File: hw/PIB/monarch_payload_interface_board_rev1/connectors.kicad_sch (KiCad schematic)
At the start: 14 parts, among them J1 5037630291, J10 5037630491, J11 5037630691, J12 5037630691, J13 5037630491, J14 5037630491, J2 5037630291, J3 5037630691, J4 5037630691, J5 5037630691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

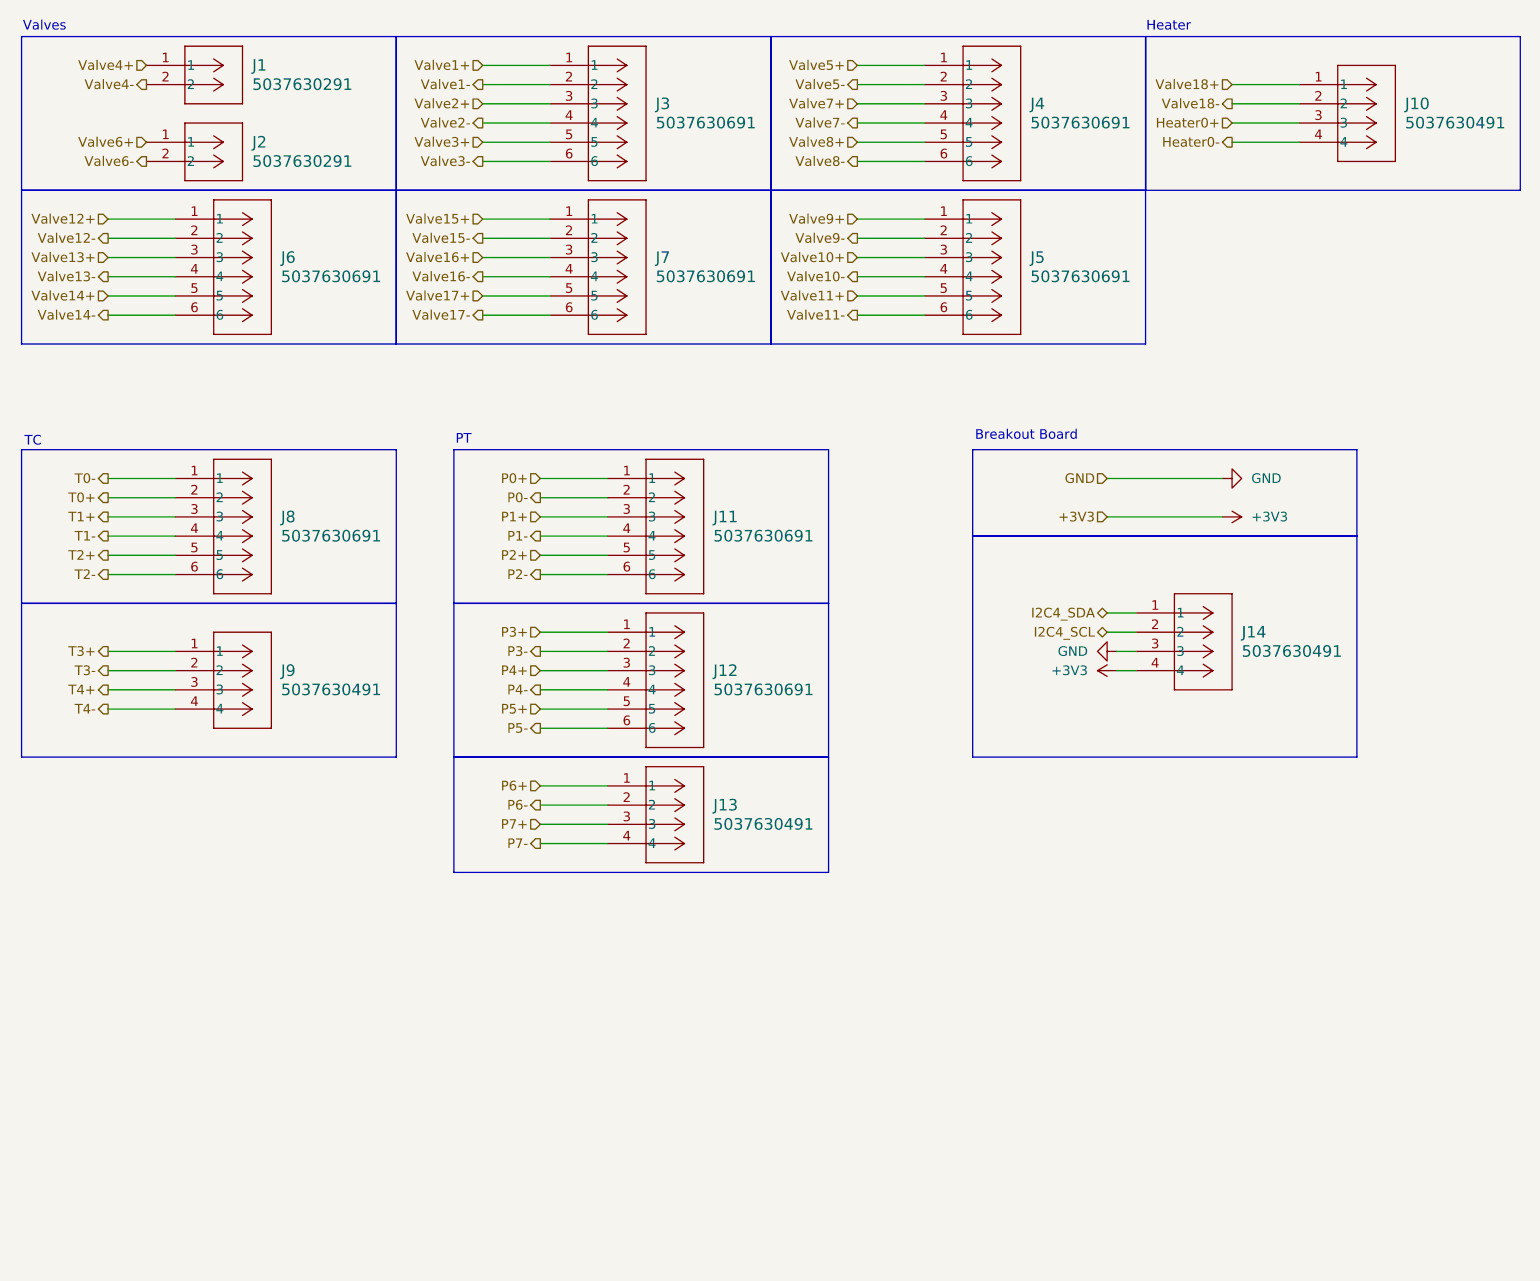
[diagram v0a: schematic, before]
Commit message: PIB layout update
done pending Ben O approval
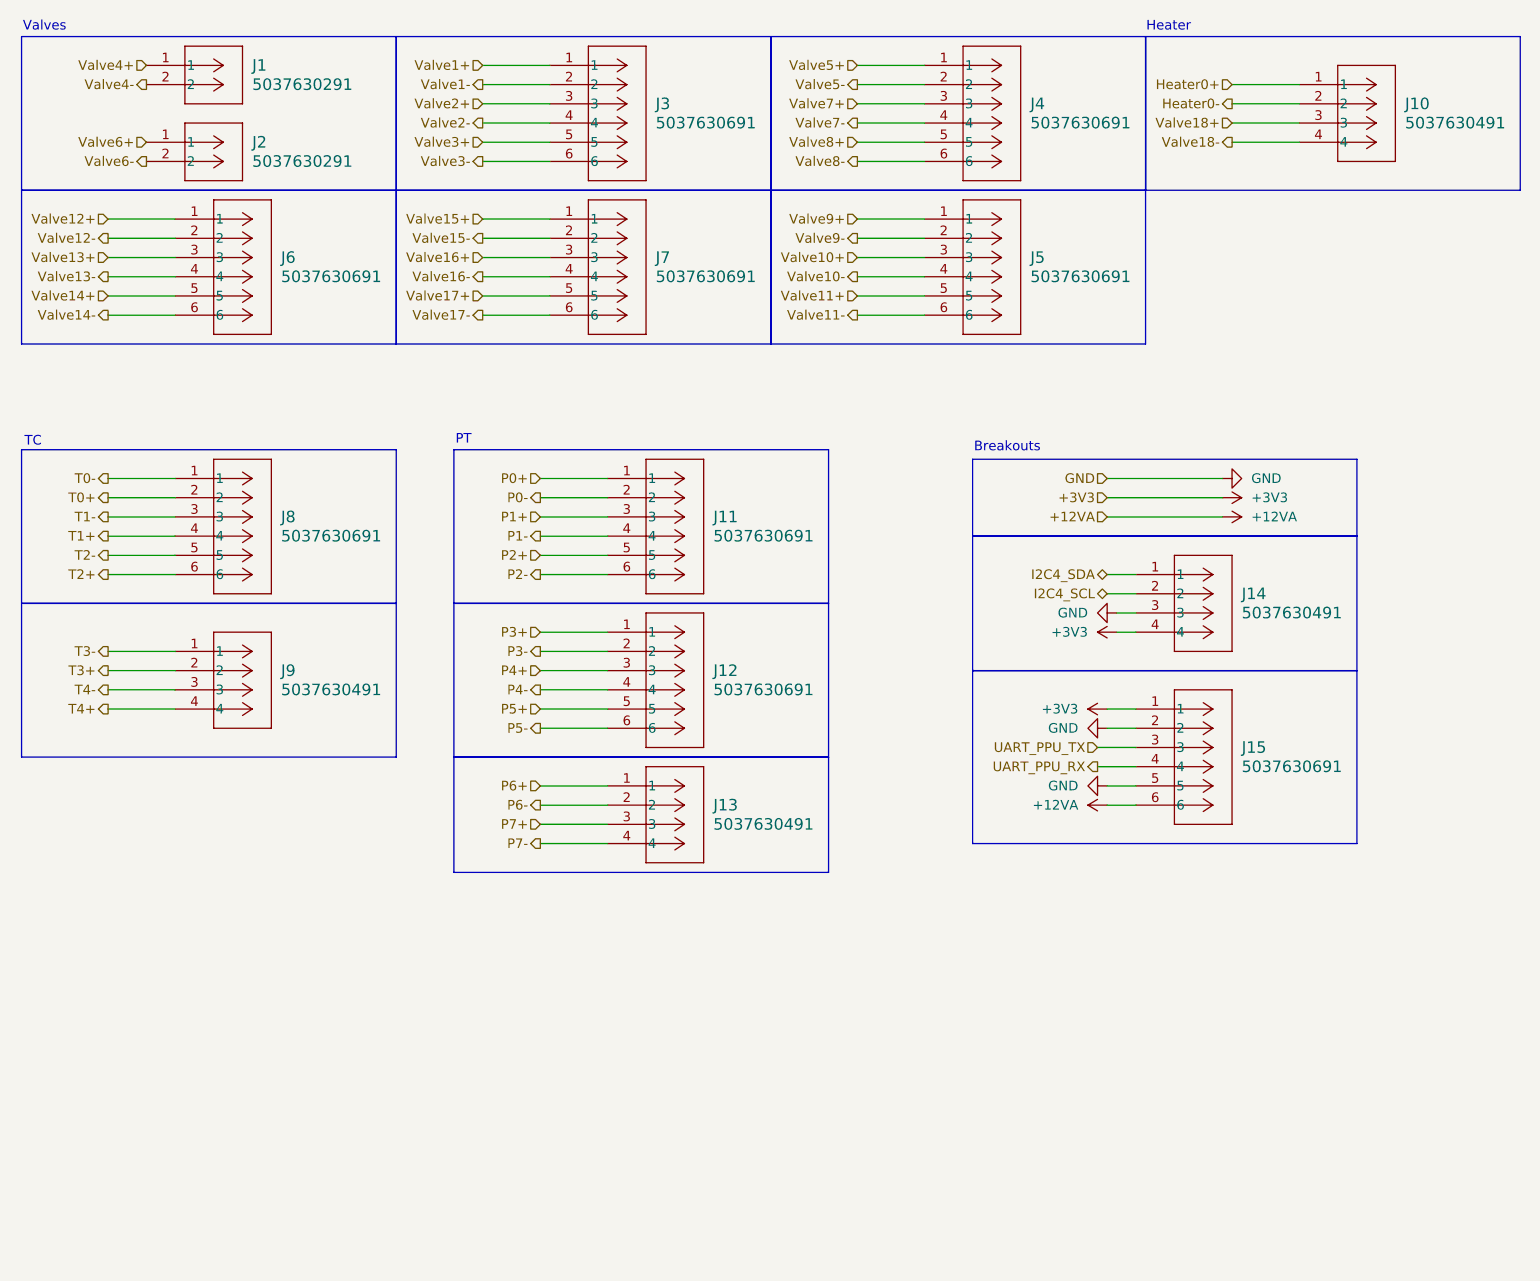
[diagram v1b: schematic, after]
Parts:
- added J15: 5037630691, CONN_5037630000-SD_06_MOL, symbol 5037630691:5037630691
- J10: footprint CONN_5037630000-SD_04_MOL -> 5037630491:CONN_5037630000-SD_04_MOL
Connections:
- net +3V3: now also J15.1
- net GND: now also J15.2, J15.5
- net Heater0+: now also J10.1; no longer J10.3
- net Heater0-: now also J10.2; no longer J10.4
- net T1+: now also J8.4; no longer J8.3
- net T1-: now also J8.3; no longer J8.4
- net T2+: now also J8.6; no longer J8.5
- net T2-: now also J8.5; no longer J8.6
- net T3+: now also J9.2; no longer J9.1
- net T3-: now also J9.1; no longer J9.2
- net T4+: now also J9.4; no longer J9.3
- net T4-: now also J9.3; no longer J9.4
- net Valve18+: now also J10.3; no longer J10.1
- net Valve18-: now also J10.4; no longer J10.2
- new net +12VA: J15.6
- new net UART_PPU_RX: J15.4
- new net UART_PPU_TX: J15.3
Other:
- note added: "Breakouts"
- note removed: "Breakout Board"
- moved on the sheet: J14

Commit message: PIB minor updates & radio board
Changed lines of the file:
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@@
 	)
 	(hierarchical_label "UART_PPU_RX"
-		(shape output)
+		(shape input)
 		(at 166.37 116.84 180)
 		(effects
@@
 	)
 	(hierarchical_label "UART_PPU_TX"
-		(shape input)
+		(shape output)
 		(at 166.37 114.3 180)
 		(effects

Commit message: minor tweaks
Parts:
- J15: footprint CONN_5037630000-SD_06_MOL -> 5037630691:CONN_5037630000-SD_06_MOL
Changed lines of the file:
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@@
 			)
 		)
-		(property "Footprint" "CONN_5037630000-SD_06_MOL"
+		(property "Footprint" "5037630691:CONN_5037630000-SD_06_MOL"
 			(at 171.45 109.22 0)
 			(effects

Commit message: BOOT PIN FIX + NRST PIN FIX
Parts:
- added J101: Conn_01x03, Connector_PinHeader_1.27mm:PinHeader_1x03_P1.27mm_Vertical, symbol Connector_Generic:Conn_01x03
- added J102: Conn_01x04, Connector_PinHeader_2.54mm:PinHeader_1x04_P2.54mm_Vertical, symbol Connector_Generic:Conn_01x04
- added J104: Conn_01x02, Connector_PinHeader_2.54mm:PinHeader_1x02_P2.54mm_Vertical, symbol Connector_Generic:Conn_01x02
- added J105: Conn_01x02, Connector_PinHeader_1.27mm:PinHeader_1x02_P1.27mm_Vertical, symbol Connector_Generic:Conn_01x02
- added J106: Conn_01x04, Connector_PinHeader_1.27mm:PinHeader_1x04_P1.27mm_Vertical, symbol Connector_Generic:Conn_01x04
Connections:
- new net BOOT: J101.2 (Pin_2)
- new net FLASH_CS: J106.1 (Pin_1)
- new net I2C_SCL: J105.1 (Pin_1)
- new net I2C_SDA: J105.2 (Pin_2)
- new net MCU_GND: J101.3 (Pin_3), J102.4 (Pin_4)
- new net MCU_V: J102.1 (Pin_1)
- new net NRST: J101.1 (Pin_1)
- new net SPI_MISO: J106.3 (Pin_3)
- new net SPI_MOSI: J106.4 (Pin_4)
- new net SPI_SCK: J106.2 (Pin_2)
- new net SWCLK: J102.2 (Pin_2)
- new net SWDIO: J102.3 (Pin_3)
- new net UART_RX: J104.1 (Pin_1)
- new net UART_TX: J104.2 (Pin_2)
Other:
- note added: "Bus Debug Pins"
- note added: "MCU Programming Pins"

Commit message: New REV2 addition
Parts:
- removed J101: Conn_01x03, Connector_PinHeader_1.27mm:PinHeader_1x03_P1.27mm_Vertical, symbol Connector_Generic:Conn_01x03
- removed J102: Conn_01x04, Connector_PinHeader_2.54mm:PinHeader_1x04_P2.54mm_Vertical, symbol Connector_Generic:Conn_01x04
- removed J104: Conn_01x02, Connector_PinHeader_2.54mm:PinHeader_1x02_P2.54mm_Vertical, symbol Connector_Generic:Conn_01x02
- removed J105: Conn_01x02, Connector_PinHeader_1.27mm:PinHeader_1x02_P1.27mm_Vertical, symbol Connector_Generic:Conn_01x02
- removed J106: Conn_01x04, Connector_PinHeader_1.27mm:PinHeader_1x04_P1.27mm_Vertical, symbol Connector_Generic:Conn_01x04
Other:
- note removed: "Bus Debug Pins"
- note removed: "MCU Programming Pins"
